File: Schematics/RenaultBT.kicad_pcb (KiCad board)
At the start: 2 copper layers, 160 x 100.3 mm, 62 parts, among them J1 PowerSupply, J2 SPDIF_Output, J3 HU_CDC_Interface, J4 Screw_Terminal_01x02, J5 Screw_Terminal_01x03, J6 Screw_Terminal_01x03, Q1 2N7000, Q2 2N7000, Q3 2N7000, Q4 2N7000, U1 LM2575-5.0BT, U2 LM3940, U3 WM8804, U4 CSRA64215, U5 74HC04, U6 STM32F103, Y1 12Mhz

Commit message: Updated PCB design
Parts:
- moved C8 2.54 mm to (146.1, 129.5)
- moved Q3 2.54 mm to (172.7, 129.5)
- moved C5 2.54 mm to (174.0, 109.2)
- moved C6 2.54 mm to (165.1, 105.4)
- moved C7 2.54 mm to (149.9, 105.4)
- moved R4 2.54 mm to (167.6, 119.4)
- moved Y1 2.54 mm to (160.0, 104.1)
- moved C9 2.54 mm to (177.8, 116.8)
- moved R3 2.54 mm to (170.2, 121.9)
- moved U3 2.54 mm to (157.5, 120.7)
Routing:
- net /HU_CDC_InterfaceAdapter/3V3: track 178.2 -> 181.8 mm
- net /I2SToSPDIF/I2S_SD_IN: track 16.5 -> 15.5 mm
- net /BTModule/I2S_WS: track 16.5 -> 15.5 mm
- net /BTModule/I2S_CLK: track 16.5 -> 15.5 mm
- net /I2SToSPDIF/DGND: track 315.2 -> 314.7 mm

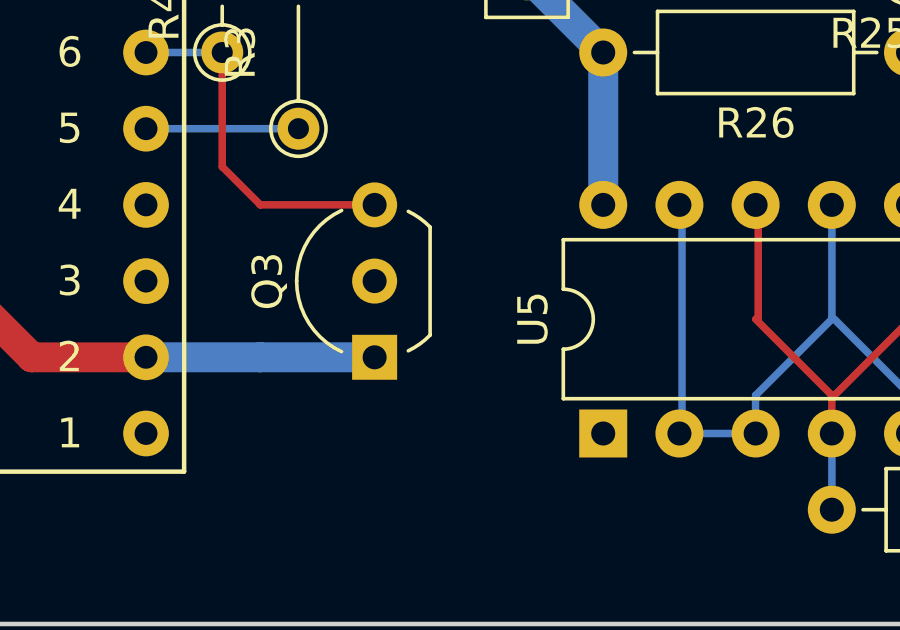
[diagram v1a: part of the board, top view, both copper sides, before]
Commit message: Added R28 to Q3 between pin 1 and 2; Updated PCB design
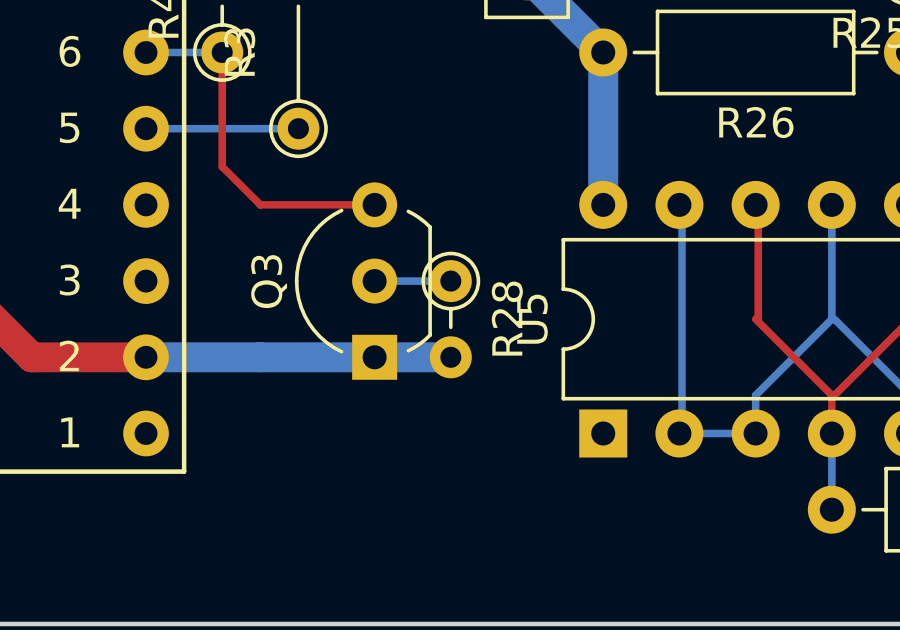
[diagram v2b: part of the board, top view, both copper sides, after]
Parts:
- added R28: 10K, Resistor_THT:R_Axial_DIN0204_L3.6mm_D1.6mm_P2.54mm_Vertical, F.Cu at (175.3, 127.0)
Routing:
- net /I2SToSPDIF/DGND: track 314.7 -> 317.2 mm
- net /I2SToSPDIF/RESETB: track 0.00 -> 2.54 mm
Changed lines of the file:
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@@
     (thickness 1.6)
     (drawings 8)
-    (tracks 210)
+    (tracks 212)
     (zones 0)
-    (modules 62)
+    (modules 63)
     (nets 46)
   )
@@
     )
   )
+  (module Resistor_THT:R_Axial_DIN0204_L3.6mm_D1.6mm_P2.54mm_Vertical (layer F.Cu)
+    (at 175.26 127 270)
+    (descr "Resistor, Axial_DIN0204 series, Axial, Vertical, pin pitch=2.54mm, 0.167W, length*diameter=3.6*1.6mm^2, http://cdn-reichelt.de/documents/datenblatt/B400/1_4W%23YAG.pdf")
+    (tags "Resistor Axial_DIN0204 series Axial Vertical pin pitch 2.54mm 0.167W length 3.6mm diameter 1.6mm")
+    (fp_text reference R28 (at 1.27 -1.92 270) (layer F.SilkS)
+      (effects (font (size 1 1) (thickness 0.15)))
+    )
+    (fp_text value 10K (at 1.27 1.92 270) (layer F.Fab)
+      (effects (font (size 1 1) (thickness 0.15)))
+    )
+    (fp_circle (center 0 0) (end 0.8 0) (layer F.Fab) (width 0.1))
+    (fp_circle (center 0 0) (end 0.92 0) (layer F.SilkS) (width 0.12))
+    (fp_line (start 0 0) (end 2.54 0) (layer F.Fab) (width 0.1))
+    (fp_line (start 0.92 0) (end 1.54 0) (layer F.SilkS) (width 0.12))
+    (fp_line (start -1.05 -1.05) (end -1.05 1.05) (layer F.CrtYd) (width 0.05))
+    (fp_line (start -1.05 1.05) (end 3.49 1.05) (layer F.CrtYd) (width 0.05))
+    (fp_line (start 3.49 1.05) (end 3.49 -1.05) (layer F.CrtYd) (width 0.05))
+    (fp_line (start 3.49 -1.05) (end -1.05 -1.05) (layer F.CrtYd) (width 0.05))
+    (fp_text user %R (at 1.27 -1.92 270) (layer F.Fab)
+      (effects (font (size 1 1) (thickness 0.15)))
+    )
+    (pad 1 thru_hole circle (at 0 0 270) (size 1.4 1.4) (drill 0.7) (layers *.Cu *.Mask)
+      (net 32 /I2SToSPDIF/RESETB))
+    (pad 2 thru_hole oval (at 2.54 0 270) (size 1.4 1.4) (drill 0.7) (layers *.Cu *.Mask)
+      (net 5 /I2SToSPDIF/DGND))
+    (model ${KISYS3DMOD}/Resistor_THT.3dshapes/R_Axial_DIN0204_L3.6mm_D1.6mm_P2.54mm_Vertical.wrl
+      (at (xyz 0 0 0))
+      (scale (xyz 1 1 1))
+      (rotate (xyz 0 0 0))
+    )
+  )
   (gr_line (start 212.09 38.1) (end 212.09 41.91) (layer B.SilkS) (width 0.2))
   (gr_line (start 212.09 138.43) (end 212.09 134.62) (layer B.SilkS) (width 0.2))
@@
   (segment (start 196.85 114.3) (end 198.12 115.57) (width 1) (layer F.Cu) (net 5))
   (segment (start 193.04 114.3) (end 196.85 114.3) (width 1) (layer F.Cu) (net 5) (status 10))
-  (segment (start 140.97 106.68) (end 146.05 106.68) (width 1) (layer B.Cu) (net 5))
+  (segment (start 140.97 106.68) (end 146.05 106.68) (width 1) (layer B.Cu) (net 5) (status 10))
   (segment (start 83.82 63.5) (end 85.09 62.23) (width 0.25) (layer F.Cu) (net 5))
   (segment (start 85.09 62.23) (end 85.09 57.15) (width 0.25) (layer F.Cu) (net 5))
-  (segment (start 81.28 63.5) (end 83.82 63.5) (width 0.25) (layer F.Cu) (net 5))
-  (segment (start 177.8 114.34) (end 166.37 114.3) (width 1) (layer F.Cu) (net 5))
-  (segment (start 177.8 114.34) (end 193.04 114.3) (width 1) (layer F.Cu) (net 5))
+  (segment (start 81.28 63.5) (end 83.82 63.5) (width 0.25) (layer F.Cu) (net 5) (status 10))
+  (segment (start 177.8 114.34) (end 166.37 114.3) (width 1) (layer F.Cu) (net 5) (status 10))
+  (segment (start 177.8 114.34) (end 193.04 114.3) (width 1) (layer F.Cu) (net 5) (status 30))
   (segment (start 146.05 104.14) (end 146.05 106.68) (width 1) (layer B.Cu) (net 5))
+  (segment (start 175.26 129.54) (end 172.72 129.54) (width 1) (layer B.Cu) (net 5))
   (segment (start 172.72 54.6775) (end 172.72 53.79) (width 0.25) (layer B.Cu) (net 6) (status 20))
   (segment (start 175.1925 57.15) (end 172.72 54.6775) (width 0.25) (layer B.Cu) (net 6))
@@
   (segment (start 129.54 119.38) (end 133.35 119.38) (width 0.25) (layer B.Cu) (net 10) (status 20))
   (segment (start 127 116.84) (end 129.54 119.38) (width 0.25) (layer B.Cu) (net 10))
-  (segment (start 148.59 114.3) (end 149.86 114.3) (width 0.25) (layer B.Cu) (net 11))
-  (segment (start 135.89 111.76) (end 144.78 111.76) (width 0.25) (layer B.Cu) (net 11))
+  (segment (start 148.59 114.3) (end 149.86 114.3) (width 0.25) (layer B.Cu) (net 11) (status 20))
+  (segment (start 135.89 111.76) (end 144.78 111.76) (width 0.25) (layer B.Cu) (net 11) (status 10))
   (segment (start 144.78 111.76) (end 148.59 115.57) (width 0.25) (layer B.Cu) (net 11))
   (segment (start 133.35 121.92) (end 130.81 121.92) (width 0.25) (layer B.Cu) (net 12) (status 10))
@@
   (segment (start 119.38 116.84) (end 119.38 100.33) (width 0.25) (layer F.Cu) (net 12))
   (segment (start 125.73 114.3) (end 133.35 114.3) (width 0.25) (layer B.Cu) (net 13) (status 30))
-  (segment (start 148.59 116.84) (end 149.86 116.84) (width 0.25) (layer B.Cu) (net 14))
-  (segment (start 135.89 114.3) (end 144.78 114.3) (width 0.25) (layer B.Cu) (net 14))
+  (segment (start 148.59 116.84) (end 149.86 116.84) (width 0.25) (layer B.Cu) (net 14) (status 20))
+  (segment (start 135.89 114.3) (end 144.78 114.3) (width 0.25) (layer B.Cu) (net 14) (status 10))
   (segment (start 144.78 114.3) (end 148.59 118.11) (width 0.25) (layer B.Cu) (net 14))
-  (segment (start 148.59 119.38) (end 149.86 119.38) (width 0.25) (layer B.Cu) (net 15))
-  (segment (start 135.89 116.84) (end 144.78 116.84) (width 0.25) (layer B.Cu) (net 15))
+  (segment (start 148.59 119.38) (end 149.86 119.38) (width 0.25) (layer B.Cu) (net 15) (status 20))
+  (segment (start 135.89 116.84) (end 144.78 116.84) (width 0.25) (layer B.Cu) (net 15) (status 10))
   (segment (start 144.78 116.84) (end 148.59 120.65) (width 0.25) (layer B.Cu) (net 15))
   (segment (start 133.35 116.84) (end 129.54 116.84) (width 0.25) (layer B.Cu) (net 16) (status 10))
@@
   (segment (start 157.48 116.84) (end 165.1 116.84) (width 1) (layer B.Cu) (net 30) (status 20))
   (segment (start 139.7 52.07) (end 128.27 52.07) (width 0.25) (layer B.Cu) (net 30) (status 30))
-  (segment (start 128.27 53.34) (end 87.63 53.34) (width 0.25) (layer F.Cu) (net 30) (status 10))
+  (segment (start 128.27 53.34) (end 87.63 53.34) (width 0.25) (layer F.Cu) (net 30))
   (segment (start 87.63 53.34) (end 86.36 54.61) (width 0.25) (layer F.Cu) (net 30))
   (segment (start 173.99 116.84) (end 170.18 116.84) (width 1) (layer B.Cu) (net 30) (status 20))
@@
   (segment (start 173.99 106.68) (end 165.1 97.79) (width 1) (layer F.Cu) (net 30))
   (segment (start 180.34 119.38) (end 180.34 124.46) (width 1) (layer B.Cu) (net 30) (status 30))
-  (segment (start 135.89 109.22) (end 143.51 109.22) (width 1) (layer B.Cu) (net 30))
-  (segment (start 85.09 66.04) (end 81.28 66.04) (width 0.25) (layer F.Cu) (net 30))
+  (segment (start 135.89 109.22) (end 143.51 109.22) (width 1) (layer B.Cu) (net 30) (status 10))
+  (segment (start 85.09 66.04) (end 81.28 66.04) (width 0.25) (layer F.Cu) (net 30) (status 20))
   (segment (start 86.36 64.77) (end 85.09 66.04) (width 0.25) (layer F.Cu) (net 30))
   (segment (start 86.36 54.61) (end 86.36 64.77) (width 0.25) (layer F.Cu) (net 30))
-  (segment (start 170.18 116.84) (end 170.18 115.57) (width 1) (layer B.Cu) (net 30))
-  (segment (start 173.99 111.76) (end 173.99 109.22) (width 1) (layer B.Cu) (net 30))
+  (segment (start 170.18 116.84) (end 170.18 115.57) (width 1) (layer B.Cu) (net 30) (status 10))
+  (segment (start 173.99 111.76) (end 173.99 109.22) (width 1) (layer B.Cu) (net 30) (status 20))
   (segment (start 170.18 115.57) (end 173.99 111.76) (width 1) (layer B.Cu) (net 30))
-  (segment (start 173.99 116.84) (end 177.8 116.84) (width 1) (layer B.Cu) (net 30))
-  (segment (start 177.8 116.84) (end 180.34 119.38) (width 1) (layer B.Cu) (net 30))
+  (segment (start 173.99 116.84) (end 177.8 116.84) (width 1) (layer B.Cu) (net 30) (status 20))
+  (segment (start 177.8 116.84) (end 180.34 119.38) (width 1) (layer B.Cu) (net 30) (status 30))
   (segment (start 143.51 104.14) (end 143.51 109.22) (width 1) (layer F.Cu) (net 30))
   (segment (start 149.86 97.79) (end 143.51 104.14) (width 1) (layer F.Cu) (net 30))
   (segment (start 195.58 110.49) (end 195.58 111.76) (width 0.25) (layer B.Cu) (net 31) (status 30))
+  (segment (start 172.72 127) (end 175.26 127) (width 0.25) (layer B.Cu) (net 32))
   (segment (start 167.64 119.38) (end 165.1 119.38) (width 0.25) (layer B.Cu) (net 33) (status 30))
   (segment (start 167.64 119.38) (end 167.64 123.19) (width 0.25) (layer F.Cu) (net 33) (status 10))

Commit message: Updated PCB design
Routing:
- net /HU_CDC_InterfaceAdapter/3V3: track 181.8 -> 179.5 mm
- net /I2SToSPDIF/DGND: track 317.2 -> 319.1 mm
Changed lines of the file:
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@@
-(kicad_pcb (version 20171130) (host pcbnew 5.0.2+dfsg1-1~bpo9+1)
+(kicad_pcb (version 20171130) (host pcbnew "(5.1.2)-1")
   (general
     (thickness 1.6)
     (drawings 8)
-    (tracks 212)
+    (tracks 214)
     (zones 0)
     (modules 63)
@@
     (zone_45_only no)
     (trace_min 0.2)
-    (segment_width 0.2)
-    (edge_width 0.15)
     (via_size 0.8)
     (via_drill 0.4)
@@
     (uvia_min_size 0.2)
     (uvia_min_drill 0.1)
+    (edge_width 0.15)
+    (segment_width 0.2)
     (pcb_text_width 0.3)
     (pcb_text_size 1.5 1.5)
@@
   (segment (start 193.04 62.23) (end 193.04 64.77) (width 0.25) (layer B.Cu) (net 4) (status 10))
   (segment (start 168.91 105.41) (end 168.99 105.49) (width 0.25) (layer B.Cu) (net 5))
-  (segment (start 149.86 127) (end 158.75 127) (width 1) (layer F.Cu) (net 5) (status 10))
-  (segment (start 158.75 127) (end 161.29 129.54) (width 1) (layer F.Cu) (net 5))
-  (segment (start 161.29 129.54) (end 165.1 129.54) (width 1) (layer F.Cu) (net 5) (status 20))
-  (segment (start 158.75 127) (end 158.75 116.84) (width 1) (layer F.Cu) (net 5))
-  (segment (start 161.29 114.3) (end 165.1 114.3) (width 1) (layer F.Cu) (net 5) (status 20))
-  (segment (start 158.75 116.84) (end 161.29 114.3) (width 1) (layer F.Cu) (net 5))
   (segment (start 180.34 50.8) (end 181.61 50.8) (width 1) (layer B.Cu) (net 5) (status 20))
   (segment (start 172.72 50.39) (end 179.93 50.39) (width 1) (layer B.Cu) (net 5) (status 10))
@@
   (segment (start 146.05 104.14) (end 146.05 106.68) (width 1) (layer B.Cu) (net 5))
   (segment (start 175.26 129.54) (end 172.72 129.54) (width 1) (layer B.Cu) (net 5))
+  (segment (start 165.1 129.54) (end 162.56 129.54) (width 1) (layer B.Cu) (net 5))
+  (segment (start 160.02 114.3) (end 165.1 114.3) (width 1) (layer B.Cu) (net 5))
+  (segment (start 154.94 124.46) (end 154.94 119.38) (width 1) (layer B.Cu) (net 5))
+  (segment (start 154.94 119.38) (end 160.02 114.3) (width 1) (layer B.Cu) (net 5))
+  (segment (start 149.86 127) (end 152.4 127) (width 1) (layer B.Cu) (net 5))
+  (segment (start 152.4 127) (end 154.94 124.46) (width 1) (layer B.Cu) (net 5))
+  (segment (start 154.94 124.46) (end 160.02 129.54) (width 1) (layer B.Cu) (net 5))
+  (segment (start 160.02 129.54) (end 162.56 129.54) (width 1) (layer B.Cu) (net 5))
   (segment (start 172.72 54.6775) (end 172.72 53.79) (width 0.25) (layer B.Cu) (net 6) (status 20))
   (segment (start 175.1925 57.15) (end 172.72 54.6775) (width 0.25) (layer B.Cu) (net 6))
@@
   (segment (start 170.18 116.84) (end 167.64 116.84) (width 1) (layer B.Cu) (net 30) (status 30))
   (segment (start 167.64 116.84) (end 165.1 116.84) (width 1) (layer B.Cu) (net 30) (status 30))
-  (segment (start 149.86 129.54) (end 153.67 129.54) (width 1) (layer B.Cu) (net 30) (status 10))
-  (segment (start 153.67 129.54) (end 154.94 128.27) (width 1) (layer B.Cu) (net 30))
-  (segment (start 154.94 128.27) (end 154.94 119.38) (width 1) (layer B.Cu) (net 30))
-  (segment (start 154.94 119.38) (end 157.48 116.84) (width 1) (layer B.Cu) (net 30))
-  (segment (start 157.48 116.84) (end 165.1 116.84) (width 1) (layer B.Cu) (net 30) (status 20))
   (segment (start 139.7 52.07) (end 128.27 52.07) (width 0.25) (layer B.Cu) (net 30) (status 30))
   (segment (start 128.27 53.34) (end 87.63 53.34) (width 0.25) (layer F.Cu) (net 30))
@@
   (segment (start 143.51 104.14) (end 143.51 109.22) (width 1) (layer F.Cu) (net 30))
   (segment (start 149.86 97.79) (end 143.51 104.14) (width 1) (layer F.Cu) (net 30))
+  (segment (start 162.56 116.84) (end 165.1 116.84) (width 1) (layer F.Cu) (net 30))
+  (segment (start 160.02 119.38) (end 162.56 116.84) (width 1) (layer F.Cu) (net 30))
+  (segment (start 160.02 124.46) (end 160.02 119.38) (width 1) (layer F.Cu) (net 30))
+  (segment (start 149.86 129.54) (end 154.94 129.54) (width 1) (layer F.Cu) (net 30))
+  (segment (start 154.94 129.54) (end 160.02 124.46) (width 1) (layer F.Cu) (net 30))
   (segment (start 195.58 110.49) (end 195.58 111.76) (width 0.25) (layer B.Cu) (net 31) (status 30))
   (segment (start 172.72 127) (end 175.26 127) (width 0.25) (layer B.Cu) (net 32))
